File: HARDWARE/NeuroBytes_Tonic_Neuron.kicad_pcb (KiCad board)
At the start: 2 copper layers, 51.9 x 18 mm, 29 parts, among them P1 CONN_01X04, P2 CONN_01X04, P3 CONN_01X04, P4 JST_GH_5-pos, Q1 Q_NPN_BEC, Q2 Q_NPN_BEC, Q3 Q_NPN_BEC, SW1 SW_PUSH, U1 STM32L011Gx, U2 TLV70033_SOT23-5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

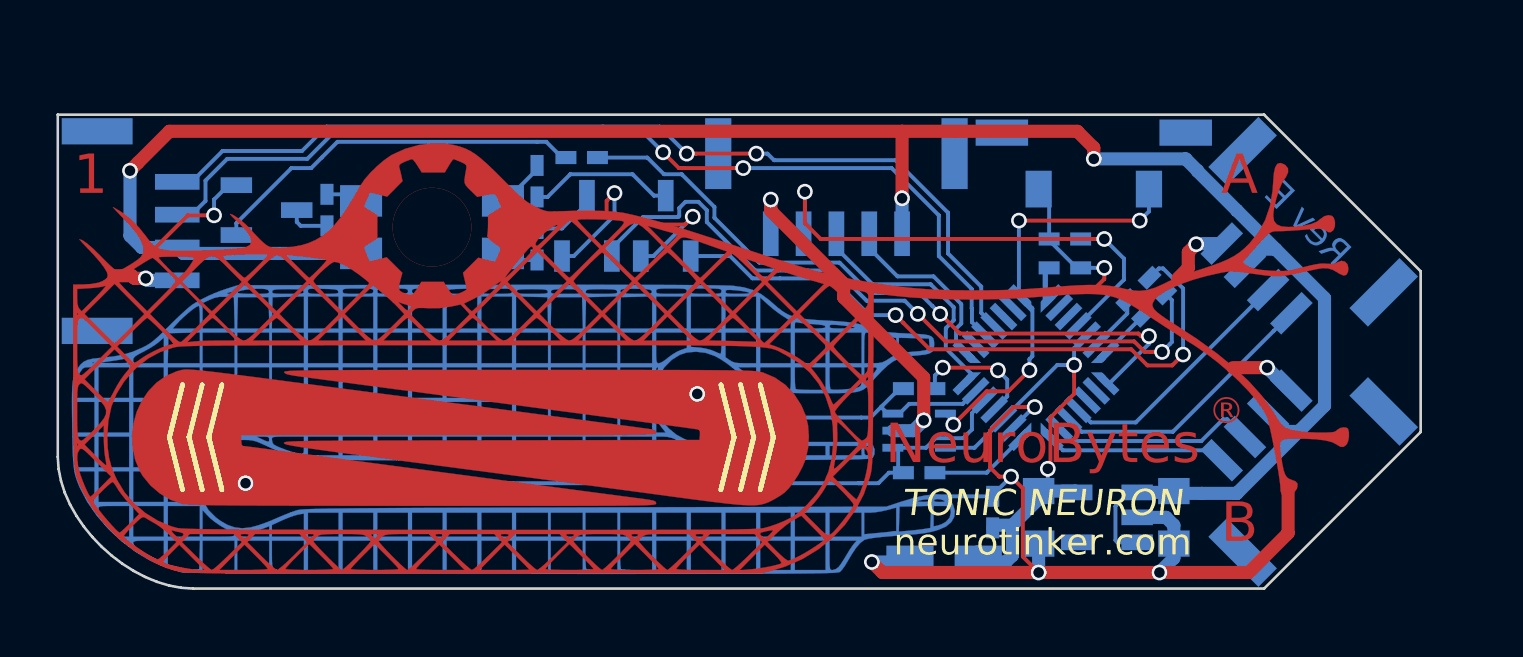
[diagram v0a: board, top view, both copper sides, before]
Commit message: updated footprints to include B.Fab outlines. minor routing changes. poured ground plane around connectors. re-generated Gerbers. added placement pdf.
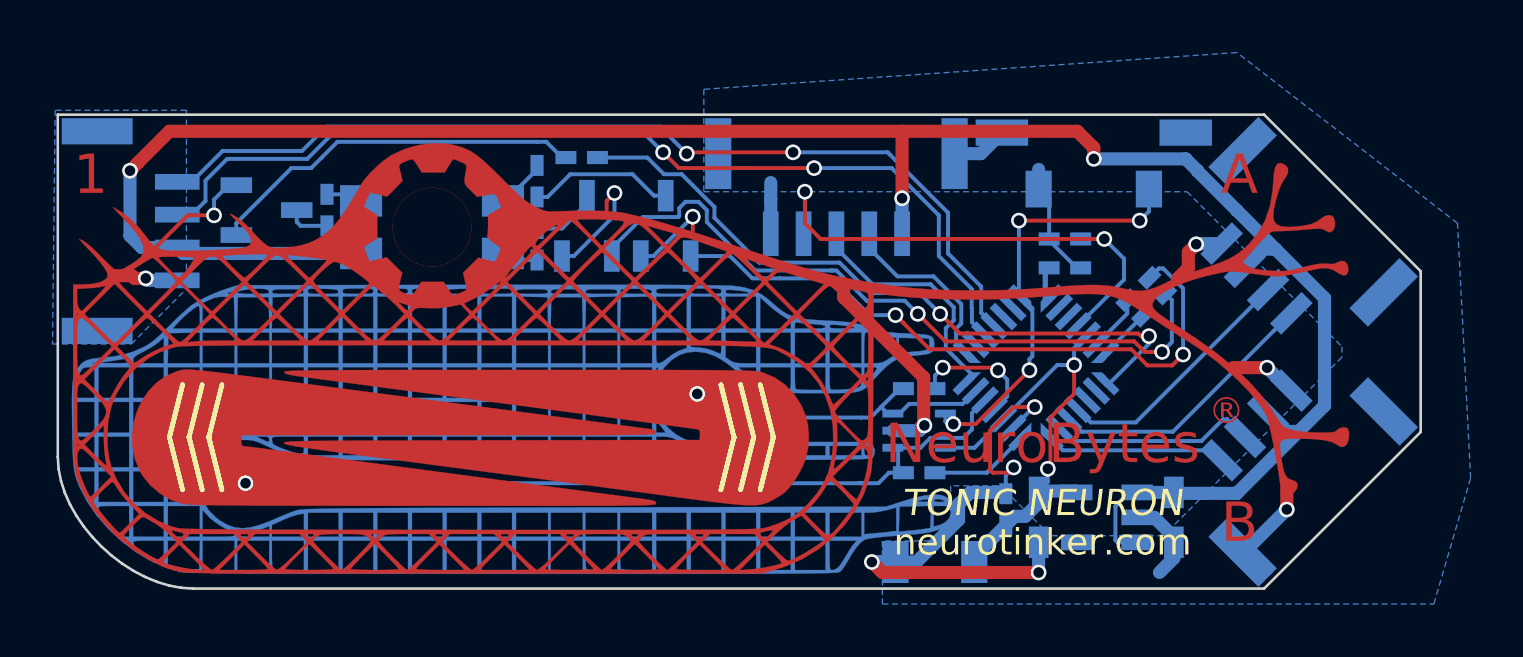
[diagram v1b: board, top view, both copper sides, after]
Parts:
- C1, C4: footprint KiCad_Footprints:ZF_SMD_NonPol_0603 -> Capacitors_SMD:C_0603_HandSoldering
- C2: footprint KiCad_Footprints:ZF_SMD_nonpol_1206 -> Capacitors_SMD:C_1206
- moved C3 0.51 mm to (189.3, 76.0)
- moved C2 0.35 mm to (186.7, 78.0)
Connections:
- P1 pad : (no net) -> GND
- P2 pad : (no net) -> GND
- P3 pad : (no net) -> GND
- P4 pad : (no net) -> GND
- SW1 pad : (no net) -> GND
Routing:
- net GND: track 78.0 -> 65.1 mm, vias 14 -> 12
- net +3V3: track 19.8 -> 18.4 mm
- added copper zone on B.Cu, net GND
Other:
- board text removed: "Rev E"
